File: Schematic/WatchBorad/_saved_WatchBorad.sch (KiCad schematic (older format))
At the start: 13 parts, among them IC1 TXS0108E, J1 Conn_01x06_Male, J2 Conn_01x09_Female, U1 E73-2G4M04S-52832, U2 FH26-13S-0.3SHW(05), U3 W25Q16BVSSIG

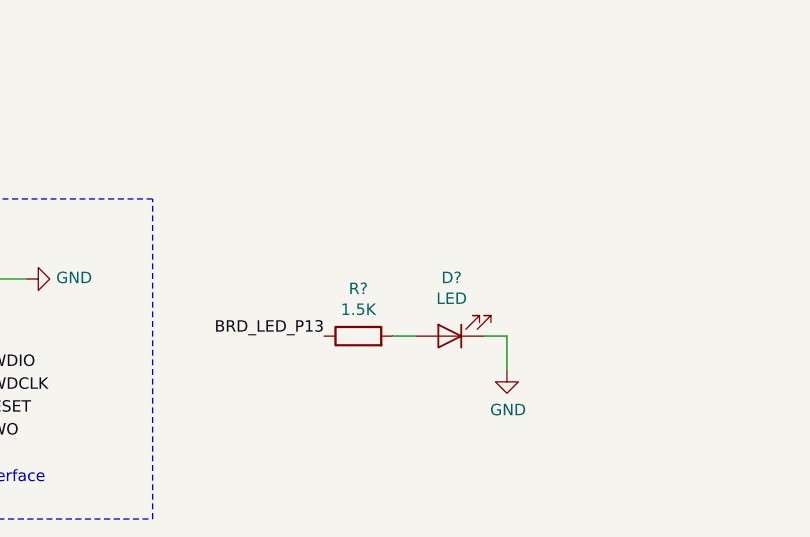
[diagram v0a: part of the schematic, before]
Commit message: Schematics changes - routed display part
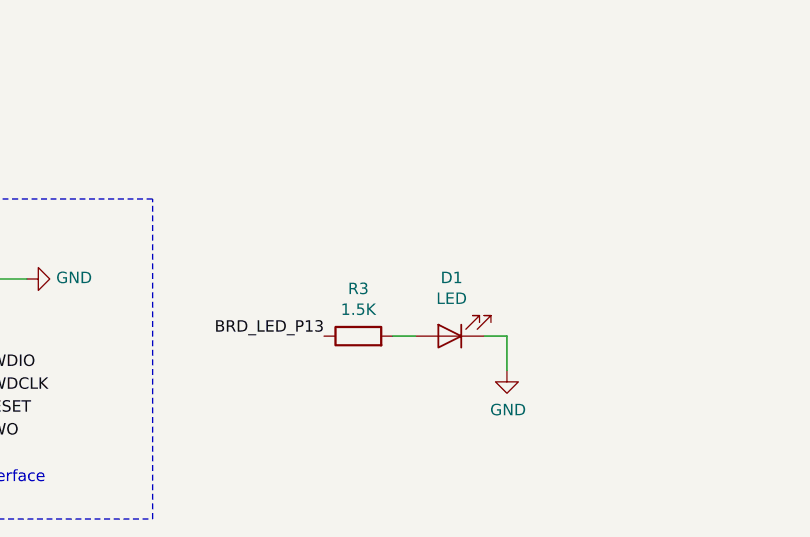
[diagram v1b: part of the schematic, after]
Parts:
- gave numbers to parts that had none: 2
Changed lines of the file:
@@
 	3750 3850 3500 3850
 $Comp
-L Device:R R?
+L Device:R R3
 U 1 1 5DB1F5A6
 P 3350 6900
-F 0 "R?" V 3557 6900 50  0000 C CNN
+F 0 "R3" V 3557 6900 50  0000 C CNN
 F 1 "1.5K" V 3466 6900 50  0000 C CNN
 F 2 "Resistor_SMD:R_0805_2012Metric_Pad1.15x1.40mm_HandSolder" V 3280 6900 50  0001 C CNN
@@
 $EndComp
 $Comp
-L Device:LED D?
+L Device:LED D1
 U 1 1 5DB1F78E
 P 3750 6900
-F 0 "D?" H 3742 6645 50  0000 C CNN
+F 0 "D1" H 3742 6645 50  0000 C CNN
 F 1 "LED" H 3742 6736 50  0000 C CNN
 F 2 "LED_SMD:LED_0805_2012Metric_Pad1.15x1.40mm_HandSolder" H 3750 6900 50  0001 C CNN
@@
 $EndComp
 $Comp
-L power:GND #PWR?
+L power:GND #PWR0122
 U 1 1 5DB1F81C
 P 4000 7050
-F 0 "#PWR?" H 4000 6800 50  0001 C CNN
+F 0 "#PWR0122" H 4000 6800 50  0001 C CNN
 F 1 "GND" H 4005 6877 50  0000 C CNN
 F 2 "" H 4000 7050 50  0001 C CNN
